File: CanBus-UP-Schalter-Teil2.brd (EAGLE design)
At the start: 50 x 50 mm, 18 parts, among them IC1 LM2937IMP-5.0, IC2 MEGA8-AI, IC3 MCP2515T-I/SO, Q1 EUROQUARTZ-MMJ, Q2 EUROQUARTZ-MMJ, Q3 BC847ASMD, Q4 BC847ASMD, U1 MCP2562-E/SN

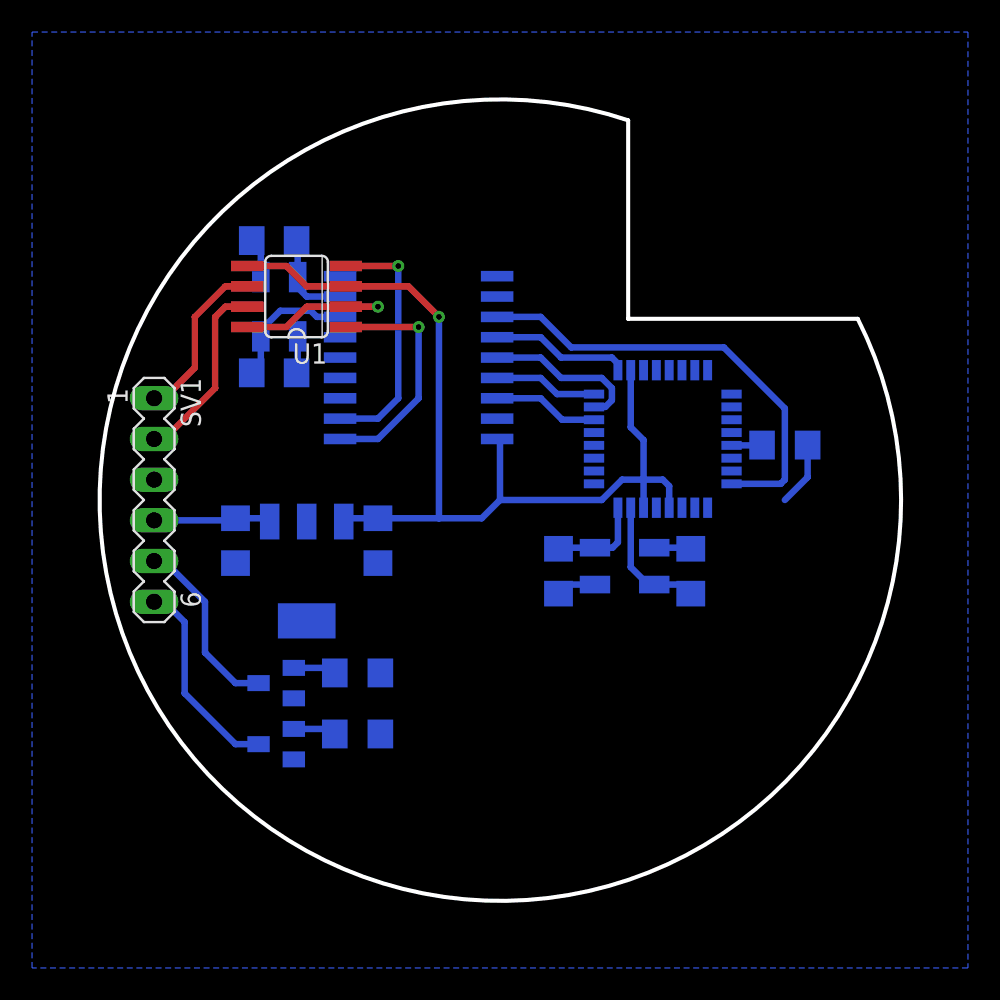
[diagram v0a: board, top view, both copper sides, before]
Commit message: Updated CAN-Bus UP-Schalter
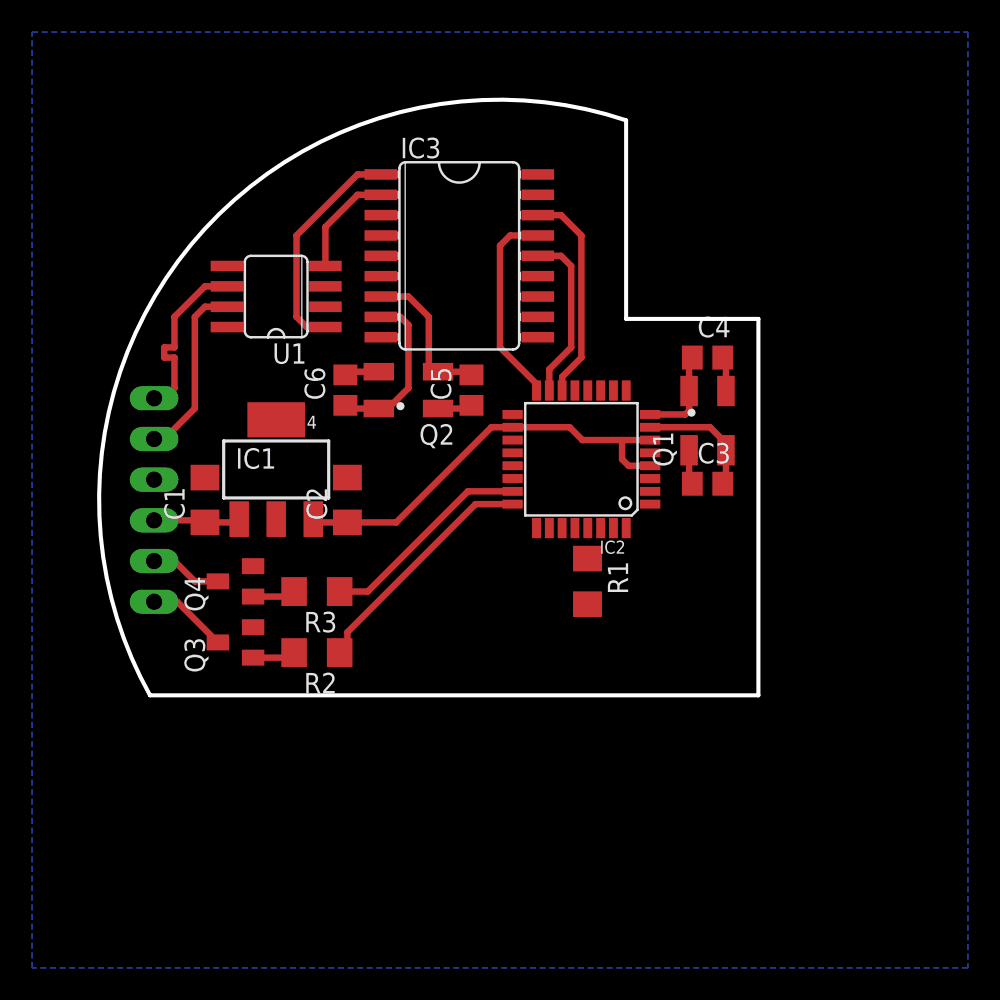
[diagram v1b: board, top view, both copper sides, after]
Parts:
- C3, C4, C5, C6: device rcl:C1206 -> rcl:R0805
- moved C4 16.3 mm to (13.0, 8.89), flipped to the top, turned to 0 degrees
- moved R1 15.0 mm to (5.46, -5.08), flipped to the top, turned to 270 degrees
- moved C5 12.4 mm to (-1.78, 6.86), flipped to the top, turned to 90 degrees
- moved Q1 10.5 mm to (13.0, 4.95), flipped to the top, turned to 90 degrees
- moved C6 10.3 mm to (-9.65, 6.86), flipped to the top, turned to 90 degrees
- moved Q2 9.60 mm to (-5.71, 6.86), flipped to the top, turned to 180 degrees
- moved IC3 6.84 mm to (-2.54, 15.2), flipped to the top, turned to 270 degrees
- moved Q3 6.84 mm to (-16.5, -8.89), flipped to the top, turned to 90 degrees
- moved Q4 6.84 mm to (-16.5, -5.08), flipped to the top, turned to 90 degrees
- moved IC1 6.63 mm to (-14.0, 1.91), flipped to the top, turned to 0 degrees
- moved R2 5.68 mm to (-11.4, -9.53), flipped to the top, turned to 180 degrees
- moved R3 5.68 mm to (-11.4, -5.71), flipped to the top, turned to 180 degrees
- moved C3 5.56 mm to (13.0, 1.02), flipped to the top, turned to 0 degrees
- moved IC2 5.24 mm to (5.08, 2.54), flipped to the top, turned to 180 degrees
- moved C2 3.17 mm to (-9.53, 0.00), flipped to the top, turned to 90 degrees
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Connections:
- removed net N$4: R3.1
- removed net N$5: R2.1
- new net PC0: IC2.23, R3.1
- new net PC1: IC2.24, R2.1
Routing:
- net +5V: track 65.6 -> 27.0 mm, vias 1 -> 0
- net INT: track 28.2 -> 0.00 mm
- net PC1: track 0.00 -> 15.4 mm
- net PC0: track 0.00 -> 13.4 mm
- net GND: track 18.4 -> 8.68 mm, vias 1 -> 0
- net RXCAN: track 15.7 -> 6.72 mm, vias 1 -> 0
- net SCK: track 8.63 -> 0.00 mm
- net RELAIS_1: track 12.8 -> 5.03 mm
- net RELAIS_2: track 11.5 -> 4.51 mm
- net CS: track 6.60 -> 13.4 mm
- net MISO: track 6.46 -> 12.6 mm
- net XTAL4: track 5.84 -> 10.5 mm
- net N$1: track 1.91 -> 0.00 mm
- net +24V: track 7.35 -> 5.45 mm
- net XTAL3: track 8.50 -> 9.53 mm
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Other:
- board size 50 x 50 mm -> 41.2 x 37.2 mm

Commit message: CAN-Schield hinzugefügt, CanBus-UP-Schalter fertiggestellt
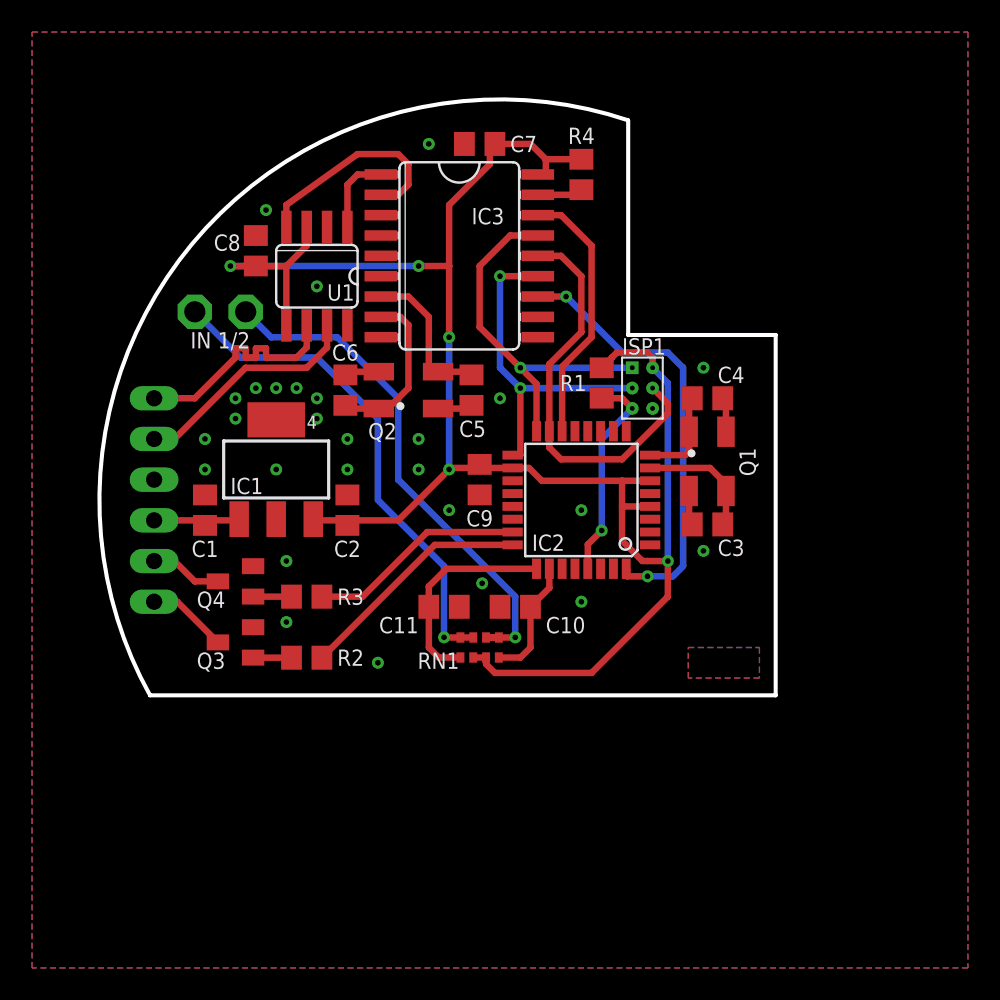
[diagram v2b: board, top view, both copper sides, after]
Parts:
- added C10, C11: (no value), rcl:C0805
- added C7, C8, C9: 100nF, rcl:C0805
- added ISP1: ISPVIAS-ONLY-1.27MM, pogo-isp:ISP-VIAS-ONLY-1.27MM
- added LSP1, LSP2: LSP13, solpad:LSP13
- added R4: 4k7, rcl:R0805
- added RN1: (no value), resistor-dil:0603-ARC
- C1, C2: device rcl:C1206 -> rcl:C0805
- C3, C4, C5, C6: device rcl:R0805 -> rcl:C0805
- R1, R2, R3: device rcl:R1206 -> rcl:R0805
- moved R1 12.4 mm to (6.35, 7.30), turned to 90 degrees
- moved U1 2.84 mm to (-11.4, 14.0), turned to 180 degrees
- moved C4 2.54 mm to (13.0, 6.35)
- moved Q1 2.54 mm to (13.0, 2.41)
- moved C3 2.54 mm to (13.0, -1.52)
- moved IC2 2.54 mm to (5.08, 0.00)
- moved R3 0.71 mm to (-12.1, -6.03)
- moved R2 0.71 mm to (-12.1, -9.84)
- moved C1 0.64 mm to (-18.4, -0.64)
- moved C2 0.64 mm to (-9.53, -0.64)
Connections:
- new net IN1: C11.1, IC2.25, RN1.5
- new net IN2: C10.1, IC2.26, RN1.8
- new net N$5: LSP1.MP, RN1.3, RN1.4
- new net N$6: LSP2.MP, RN1.1, RN1.2
- new net RST: IC2.29, ISP1.RST, R1.1
- net +5V: now also C7.1, C8.1, C9.1, ISP1.VCC, R4.2, RN1.6, RN1.7
- net GND: now also C10.2, C11.2, C7.2, C8.2, C9.2, ISP1.GND
- net MISO: now also ISP1.MISO
- net MOSI: now also ISP1.MOSI
- net N$1: now also IC3.17, R4.1; no longer IC2.29, R1.1
- net SCK: now also ISP1.SCK
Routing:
- net +5V: track 27.0 -> 118.8 mm, vias 0 -> 5
- net N$6: track 0.00 -> 32.3 mm, vias 0 -> 1
- net N$5: track 0.00 -> 31.4 mm, vias 0 -> 1
- net INT: track 0.00 -> 27.5 mm, vias 0 -> 2
- net SCK: track 0.00 -> 21.5 mm, vias 0 -> 2
- net MOSI: track 10.7 -> 25.6 mm
- net RST: track 0.00 -> 13.3 mm, vias 0 -> 1
- net IN1: track 0.00 -> 13.2 mm
- net MISO: track 12.6 -> 23.2 mm, vias 0 -> 1
- net TXCAN: track 14.0 -> 4.99 mm
- net IN2: track 0.00 -> 7.64 mm
- net RXCAN: track 6.72 -> 13.5 mm
- net CANL: track 11.3 -> 14.5 mm
- net CANH: track 11.3 -> 14.5 mm
- net CS: track 13.4 -> 16.5 mm
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- added copper zone on layer 16, net BOT
- added copper zone on layer 1, net GND
- added copper zone on layer 1, net TOP
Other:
- board size 41.2 x 37.2 mm -> 42.2 x 37.2 mm
- board text added: "BOT"
- board text added: "IN 1/2"
- board text added: "TOP"

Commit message: CanBus-UP-Schalter fertiggestellt
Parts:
- added +5V, +5V1, PB0, PB1, PC4, PC5, PD7: LSP13, solpad:LSP13
- added R5, R6: 4k7, rcl:R0805
- moved R1 5.55 mm to (11.1, 10.2), turned to 0 degrees
- moved C10 3.27 mm to (3.81, -8.26), turned to 0 degrees
- moved C11 1.62 mm to (-3.81, -8.26), turned to 180 degrees
- moved RN1 1.59 mm to (0.00, -8.26)
- moved LSP1 0.71 mm to (-18.4, 11.4)
- moved LSP2 0.32 mm to (-15.9, 11.4)
- renumbered ISP1 to ISP
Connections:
- new net N$10: IC2.28, PC5.MP, R6.1
- new net N$11: IC2.27, PC4.MP, R5.1
- new net N$7: IC2.13, PB1.MP
- new net N$8: IC2.12, PB0.MP
- new net N$9: IC2.11, PD7.MP
- net +5V: now also +5V.MP, +5V1.MP, R5.2, R6.2
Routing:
- net N$10: track 0.00 -> 40.1 mm, vias 0 -> 2
- net N$11: track 0.00 -> 39.4 mm
- net N$9: track 0.00 -> 16.9 mm
- net +5V: track 118.8 -> 135.2 mm, vias 5 -> 6
- net N$8: track 0.00 -> 14.2 mm
- net N$7: track 0.00 -> 10.3 mm
- net RST: track 13.3 -> 18.3 mm
- net N$6: track 32.3 -> 27.7 mm
- net IN1: track 13.2 -> 10.4 mm
- net N$5: track 31.4 -> 28.9 mm
- net IN2: track 7.64 -> 5.97 mm
- net MISO: track 23.2 -> 22.2 mm
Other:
- board size 42.2 x 37.2 mm -> 42.2 x 37.1 mm
- board text added: "+5V"

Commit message: Werte von Bauteilen angepasst
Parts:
- C1, C10, C11: value (none) -> 100nF
- C2: value (none) -> 10µF Low ESR
- RN1: value (none) -> 10k
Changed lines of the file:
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@@
 </autorouter>
 <elements>
-<element name="C1" library="rcl" package="C0805" value="" x="-18.415" y="-0.635" smashed="yes" rot="R90">
+<element name="C1" library="rcl" package="C0805" value="100nF" x="-18.415" y="-0.635" smashed="yes" rot="R90">
 <attribute name="NAME" x="-18.415" y="-2.54" size="1.016" layer="25" font="vector" align="top-center"/>
 <attribute name="VALUE" x="-15.875" y="-1.905" size="1.27" layer="27" rot="R90"/>
 </element>
-<element name="C2" library="rcl" package="C0805" value="" x="-9.525" y="-0.635" smashed="yes" rot="R90">
+<element name="C2" library="rcl" package="C0805" value="10µF Low ESR" x="-9.525" y="-0.635" smashed="yes" rot="R90">
 <attribute name="NAME" x="-9.525" y="-2.54" size="1.016" layer="25" font="vector" align="top-center"/>
 <attribute name="VALUE" x="-6.985" y="-1.905" size="1.27" layer="27" rot="R90"/>
@@
 <attribute name="VALUE" x="7.62" y="19.685" size="1.27" layer="27" rot="R90"/>
 </element>
-<element name="RN1" library="resistor-dil" package="0603-ARC" value="" x="0" y="-8.255" smashed="yes" rot="R180">
+<element name="RN1" library="resistor-dil" package="0603-ARC" value="10k" x="0" y="-8.255" smashed="yes" rot="R180">
 <attribute name="OC_NEWARK" value="unknown" x="0" y="-8.255" size="1.778" layer="27" rot="R180" display="off"/>
 <attribute name="OC_FARNELL" value="unknown" x="0" y="-8.255" size="1.778" layer="27" rot="R180" display="off"/>
@@
 <attribute name="VALUE" x="1.905" y="-9.525" size="1.27" layer="27" ratio="10" rot="R180"/>
 </element>
-<element name="C10" library="rcl" package="C0805" value="" x="3.81" y="-8.255" smashed="yes">
+<element name="C10" library="rcl" package="C0805" value="100nF" x="3.81" y="-8.255" smashed="yes">
 <attribute name="NAME" x="3.81" y="-9.525" size="1.016" layer="25" font="vector" align="top-center"/>
 <attribute name="VALUE" x="2.54" y="-10.795" size="1.27" layer="27"/>
 </element>
-<element name="C11" library="rcl" package="C0805" value="" x="-3.81" y="-8.255" smashed="yes" rot="R180">
+<element name="C11" library="rcl" package="C0805" value="100nF" x="-3.81" y="-8.255" smashed="yes" rot="R180">
 <attribute name="NAME" x="-3.81" y="-9.525" size="1.016" layer="25" font="vector" align="top-center"/>
 <attribute name="VALUE" x="-2.54" y="-5.715" size="1.27" layer="27" rot="R180"/>
